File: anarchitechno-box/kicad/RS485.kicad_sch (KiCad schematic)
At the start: 10 parts, among them J9 Screw_Terminal_01x02, U2 MAX485E

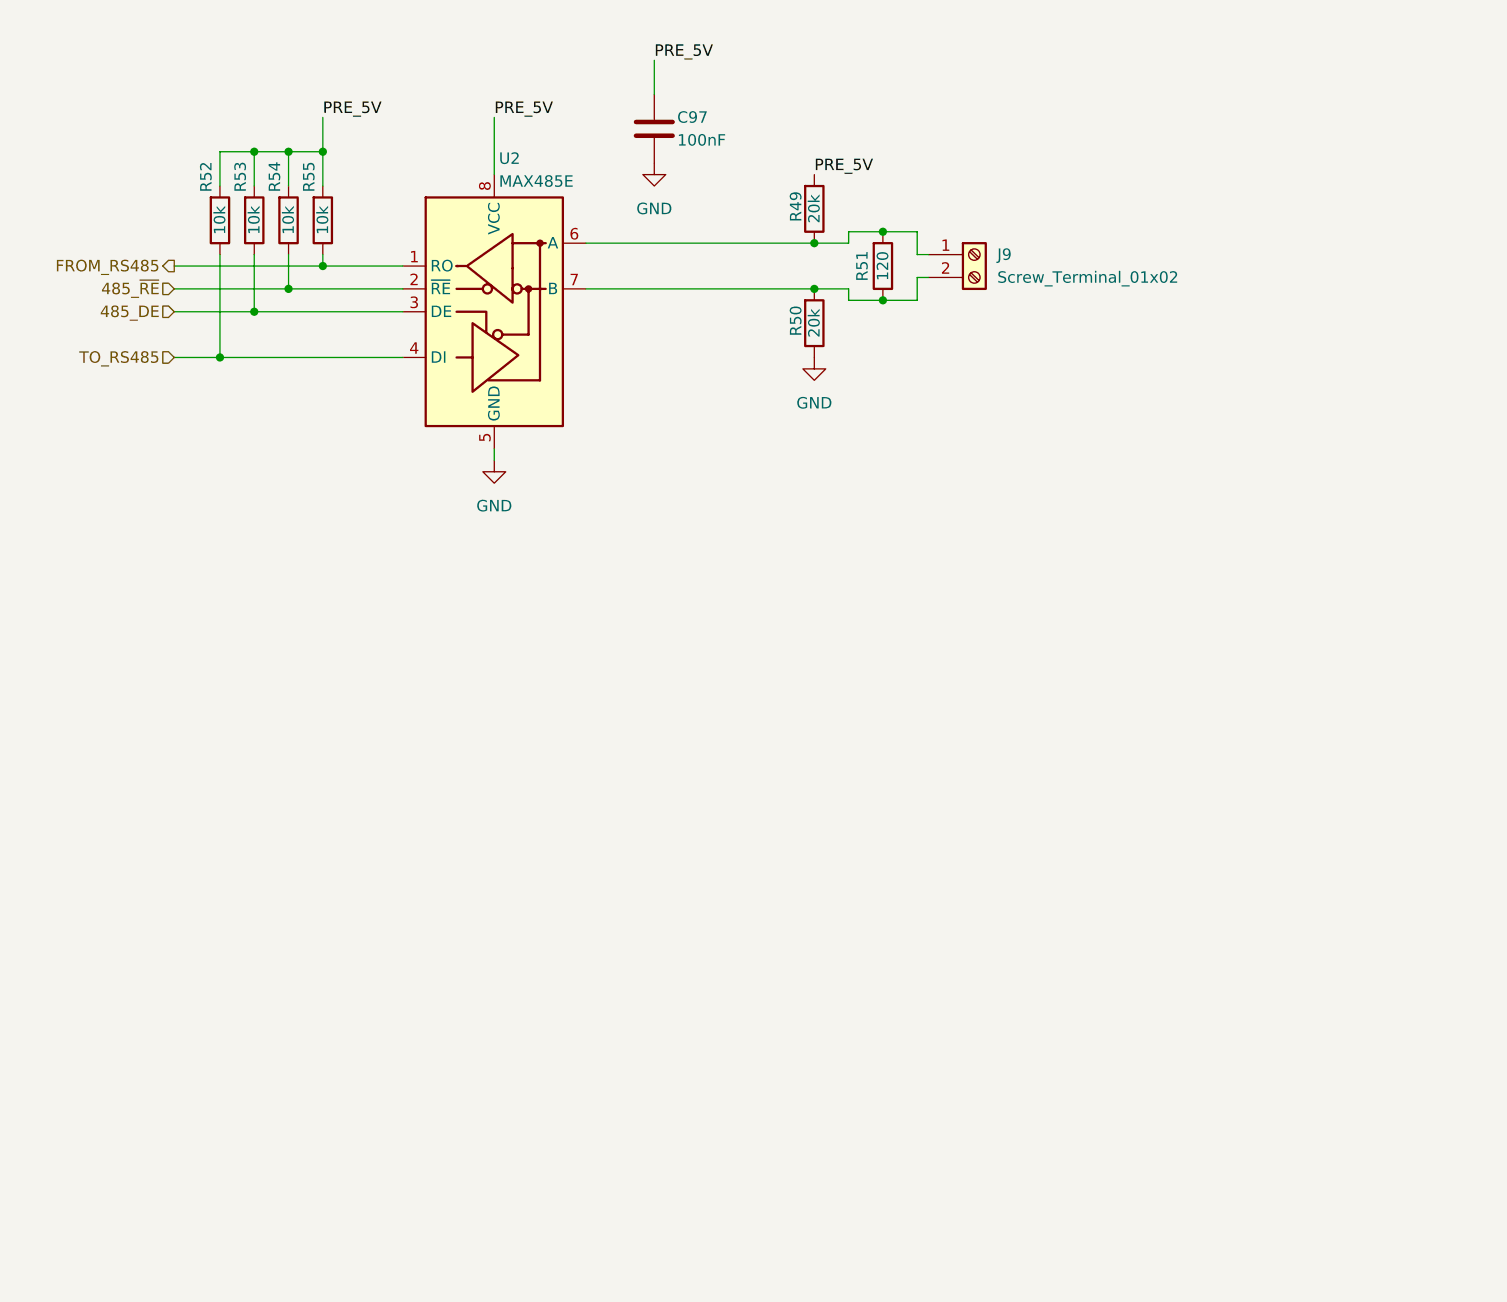
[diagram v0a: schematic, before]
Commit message: Schematic & PCB changes: - Cleaned up unnecessary electrolytic input capacitor flyback - Removed dual diode rectification on 5V, increased output capacitors - Feedback resistors DC/DCs set, enlarged for JLC basic parts - Sweep through schematic to consolidate caps to JLC basic parts (see list schematic front page) - Midi OUTPUT added (please check schematic) - Wiznet W5500 schematic reworked to RJ45 reference schematic: https://docs.wiznet.io/assets/files/w5500_sch_v110_use_mag_-dfff8bbb103d13be4f25cd2b2f8b950d.pdf - Replaced ethernet jack to HR911105A - Crystals chosen for W5500 and RP2350B (according to reference), 15pF load caps. - RS485 driver changed to SP3485EN for 3.3V operation - Replaced RS485 bus connectors with 2x RJ45s for passthrough - Groove connector replaced with JST XH 2mm - Added LCSC part numbers for various components in the schematic
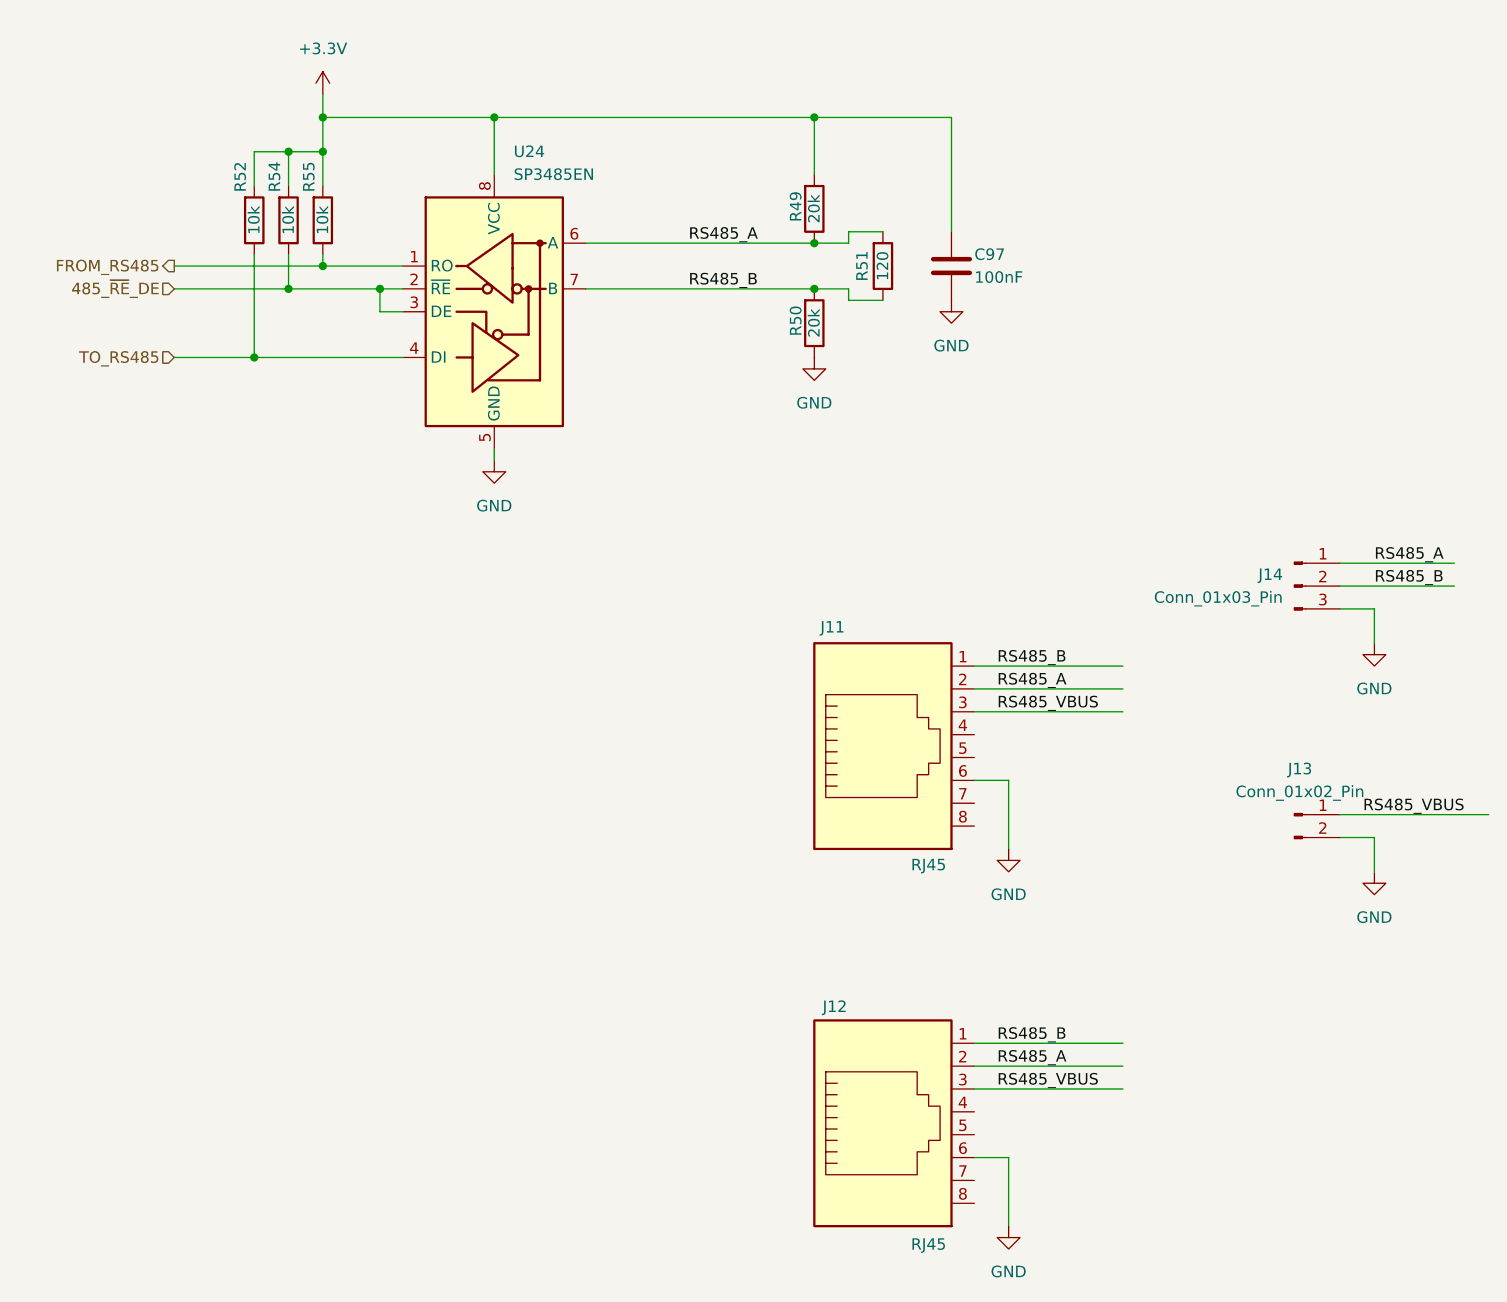
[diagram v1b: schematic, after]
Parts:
- removed J9: Screw_Terminal_01x02, TerminalBlock_Phoenix:TerminalBlock_Phoenix_PT-1,5-2-5.0-H_1x02_P5.00mm_Horizontal, symbol Connector:Screw_Terminal_01x02
- removed R53: 10k, Resistor_SMD:R_0402_1005Metric, symbol Device:R
- removed U2: MAX485E, Package_SO:SOIC-8_3.9x4.9mm_P1.27mm, symbol Interface_UART:MAX485E
- added J11, J12: RJ45, Connector_RJ:RJ45_Amphenol_54602-x08_Horizontal, symbol Connector:RJ45
- added J13: Conn_01x02_Pin, Connector_PinHeader_2.54mm:PinHeader_1x02_P2.54mm_Vertical, symbol Connector:Conn_01x02_Pin
- added J14: Conn_01x03_Pin, Connector_JST:JST_XH_B3B-XH-AM_1x03_P2.50mm_Vertical, symbol Connector:Conn_01x03_Pin
- added U24: SP3485EN, Package_SO:SOIC-8_3.9x4.9mm_P1.27mm, symbol Interface_UART:SP3485EN
- R49, R50: footprint Resistor_SMD:R_0402_1005Metric -> Resistor_SMD:R_0603_1608Metric; LCSC Part (none) -> C25765
- R51: footprint Resistor_SMD:R_0402_1005Metric -> Resistor_SMD:R_0805_2012Metric; LCSC Part (none) -> C17415
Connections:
- net FROM_RS485: now also U24.1 (RO)
- net GND: now also J11.6, J12.6, J13.2 (Pin_2), J14.3 (Pin_3), U24.5 (GND)
- net TO_RS485: now also U24.4 (DI)
- net RS485_B: now reaches R50.2, R51.1
- net RS485_B: now also J11.1, J12.1, J14.2 (Pin_2), U24.7 (B)
- net RS485_A: now reaches R49.1, R51.2
- net RS485_A: now also J11.2, J12.2, J14.1 (Pin_1), U24.6 (A)
- net 485_~{RE} renamed 485_~{RE}_DE
- net 485_~{RE}_DE: now also U24.2 (~{RE}), U24.3 (DE)
- net PRE_5V renamed +3.3V
- net +3.3V: now also U24.8 (VCC)
- new net RS485_VBUS: J11.3, J12.3, J13.1 (Pin_1)
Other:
- moved on the sheet: C97, R52

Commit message: - Thermische berekening DRV8245 vs losse transistors - DRV8245 package gecorrigeerd naar TSSOP-28 - Layout aangepast om grotere package te passen - 1x GND output per kanaal - Waarschijnlijk geen 140mm fan nodig => print weer gekropmen - RS485 power line gefixed (3.3V vs 3V3P) - Kleine BOM en I/O wijzigingen tbv layout
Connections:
- net +3.3V renamed +3V3
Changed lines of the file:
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@@
+	)
+	(symbol
+		(lib_id "power:+3.3V")
+		(at 52.07 46.99 0)
+		(unit 1)
+		(exclude_from_sim no)
+		(in_bom yes)
+		(on_board yes)
+		(dnp no)
+		(property "Reference" "#PWR0186"
+			(at 52.07 50.8 0)
+			(effects
+				(font
+					(size 1.27 1.27)
+				)
+				(hide yes)
+			)
+		)
+		(property "Value" "+3V3"
+			(at 52.07 44.45 90)
+			(effects
+				(font
+					(size 1.27 1.27)
+				)
+				(justify left)
+			)
+		)
+		(property "Footprint" ""
+			(at 52.07 46.99 0)
+			(effects
+				(font
+					(size 1.27 1.27)
+				)
+				(hide yes)
+			)
+		)
+		(property "Datasheet" ""
+			(at 52.07 46.99 0)
+			(effects
+				(font
+					(size 1.27 1.27)
+				)
+				(hide yes)
+			)
+		)
+		(property "Description" "Power symbol creates a global label with name \"+3.3V\""
+			(at 52.07 46.99 0)
+			(effects
+				(font
+					(size 1.27 1.27)
+				)
+				(hide yes)
+			)
+		)
+		(pin "1"
+		)
+		(instances
+			(project "anarchytechnobox"
+				(path "/8c734c41-38ed-40fc-83bd-134786dcfb35/4ac30784-1697-4f10-a090-83a6b536d188"
+					(reference "#PWR0186")
+					(unit 1)
+				)
+			)
+		)
 	)
 	(symbol
@@
 					(unit 1)
 				)
-			)
-		)
-	)
-	(symbol
-		(lib_id "power:+3.3V")
-		(at 52.07 46.99 0)
-		(unit 1)
-		(exclude_from_sim no)
-		(in_bom yes)
-		(on_board yes)
-		(dnp no)
-		(fields_autoplaced yes)
-		(property "Reference" "#PWR0186"
-			(at 52.07 50.8 0)
-			(effects
-				(font
-					(size 1.27 1.27)
-				)
-				(hide yes)
-			)
-		)
-		(property "Value" "+3.3V"
-			(at 52.07 41.91 0)
-			(effects
-				(font
-					(size 1.27 1.27)
-				)
-			)
-		)
-		(property "Footprint" ""
-			(at 52.07 46.99 0)
-			(effects
-				(font
-					(size 1.27 1.27)
-				)
-				(hide yes)
-			)
-		)
-		(property "Datasheet" ""
-			(at 52.07 46.99 0)
-			(effects
-				(font
-					(size 1.27 1.27)
-				)
-				(hide yes)
-			)
-		)
-		(property "Description" "Power symbol creates a global label with name \"+3.3V\""
-			(at 52.07 46.99 0)
-			(effects
-				(font
-					(size 1.27 1.27)
-				)
-				(hide yes)
-			)
-		)
-		(pin "1"
-		)
-		(instances
-			(project ""
-				(path "/8c734c41-38ed-40fc-83bd-134786dcfb35/4ac30784-1697-4f10-a090-83a6b536d188"
-					(reference "#PWR0186")
-					(unit 1)
-				)

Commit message: BOM nagelopen, bestelklaar.
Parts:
- J11, J12: LCSC Part (none) -> C86577
- J13, J14: now left out of the parts list
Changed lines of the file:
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@@
 		(unit 1)
 		(exclude_from_sim no)
-		(in_bom yes)
+		(in_bom no)
 		(on_board yes)
 		(dnp no)
@@
 		(unit 1)
 		(exclude_from_sim no)
-		(in_bom yes)
+		(in_bom no)
 		(on_board yes)
 		(dnp no)
@@
 			)
 		)
+		(property "LCSC Part" "C86577"
+			(at 114.3 160.02 0)
+			(effects
+				(font
+					(size 1.27 1.27)
+				)
+				(hide yes)
+			)
+		)
 		(pin "7"
 		)
@@
 			(at 114.3 118.11 0)
 			(effects
+				(font
+					(size 1.27 1.27)
+				)
+				(hide yes)
+			)
+		)
+		(property "LCSC Part" "C86577"
+			(at 114.3 118.11 0)
+			(effects
